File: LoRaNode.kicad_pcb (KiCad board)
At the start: 2 copper layers, 45 x 53 mm, 34 parts, among them J1 Conn_01x09, J2 Conn_01x03, J3 Conn_01x01, J4 ISP, J5 Conn_01x06, J6 Conn_01x01, J8 D2, J9 D3, SW1 SW_Push, U1 RFM95W-868S2, U4 ATMEGA328P-AU, Y1 8MHz HC5032/4

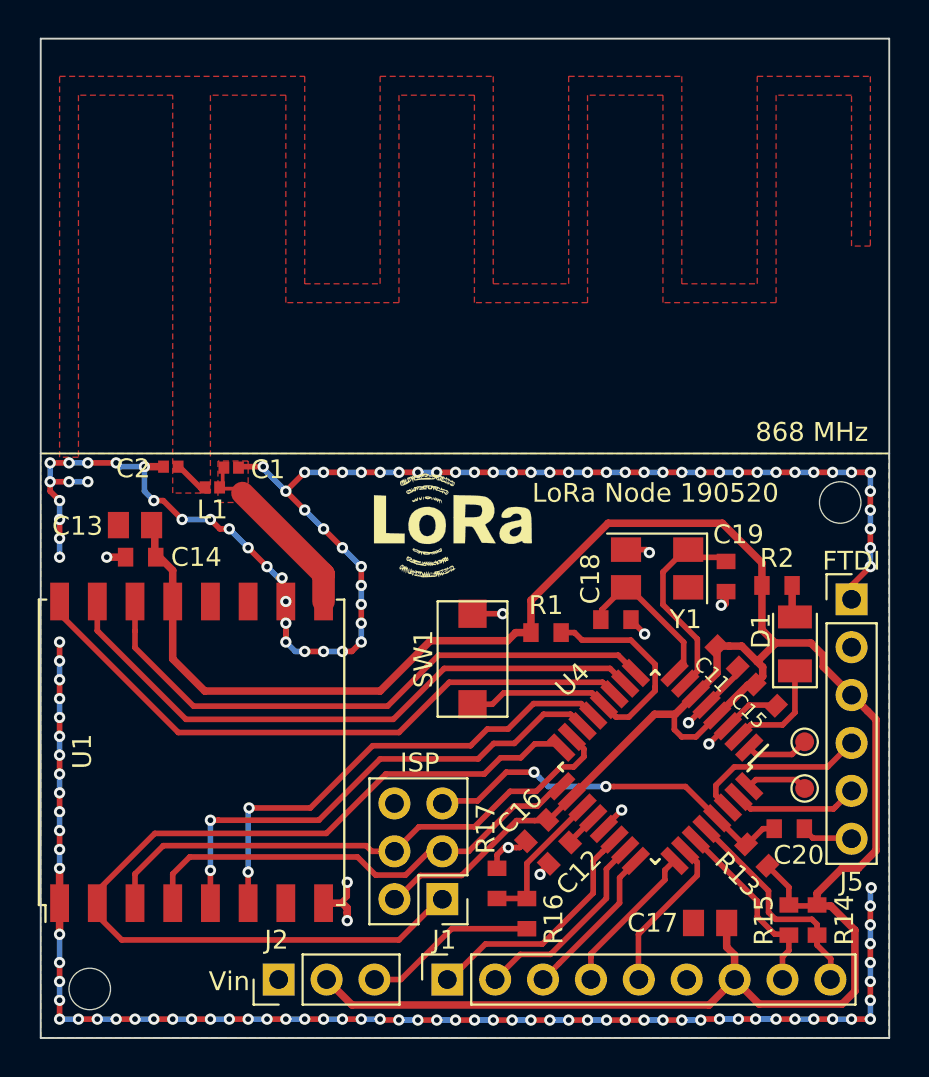
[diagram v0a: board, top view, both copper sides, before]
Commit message: Anotation reset, added BOM
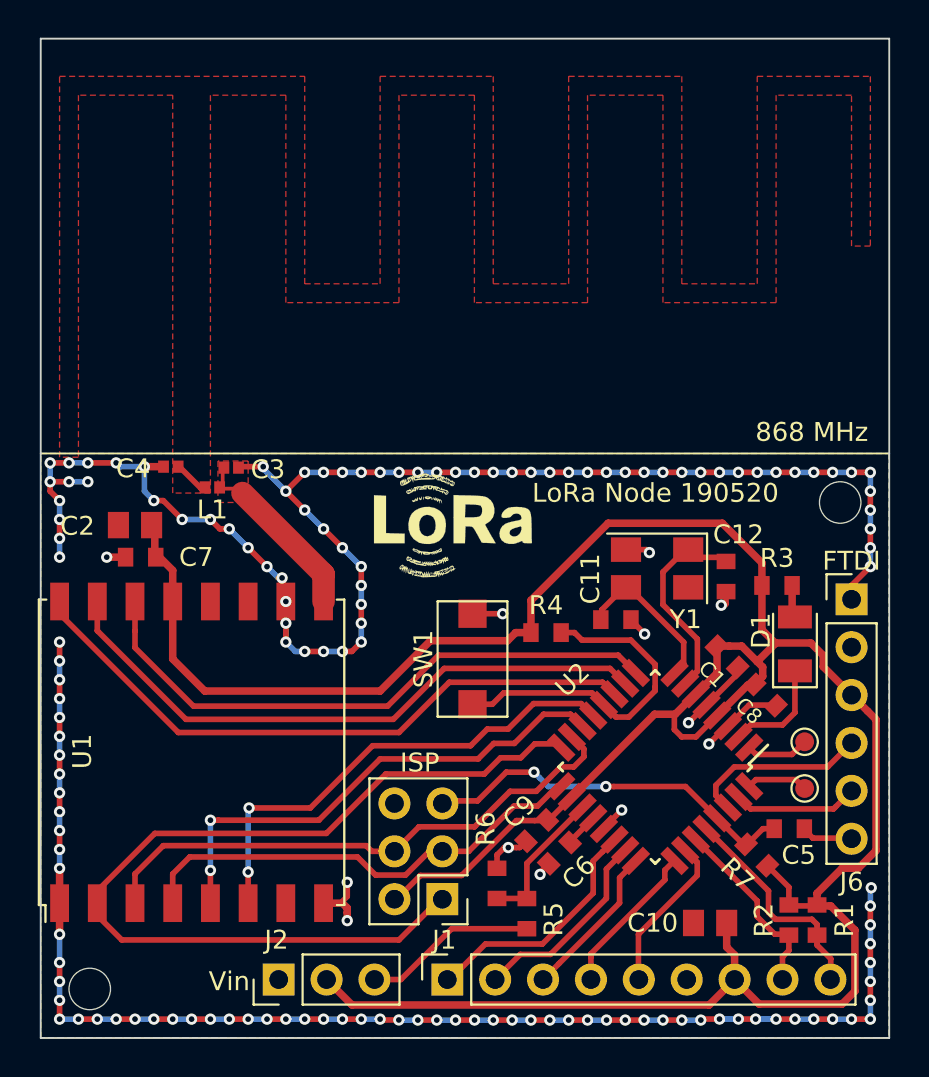
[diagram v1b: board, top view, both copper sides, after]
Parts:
- renumbered C11 to C1, C17 to C10, C18 to C11, C19 to C12, C13 to C2, C1 to C3, C2 to C4, C20 to C5, C12 to C6, C14 to C7, C15 to C8, C16 to C9, J4 to J3, J8 to J4, J9 to J5, J5 to J6, J3 to J7, J6 to J8, R14 to R1, R15 to R2, R2 to R3, R1 to R4, R16 to R5, R17 to R6, R13 to R7, U4 to U2

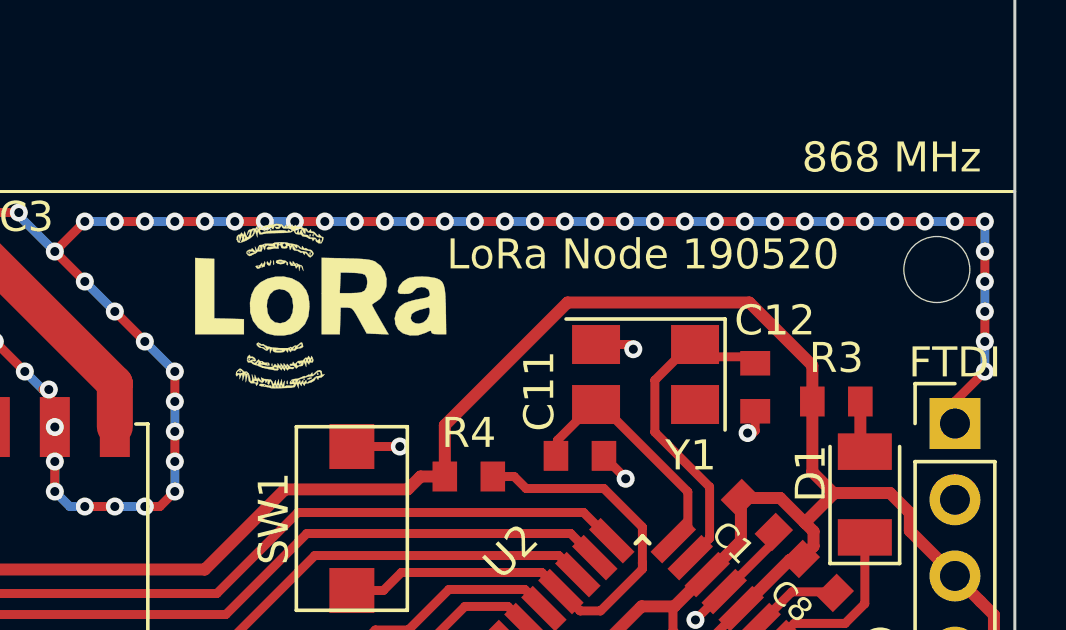
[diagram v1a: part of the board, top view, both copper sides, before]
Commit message: Corrected silk layer, removed old footprint files
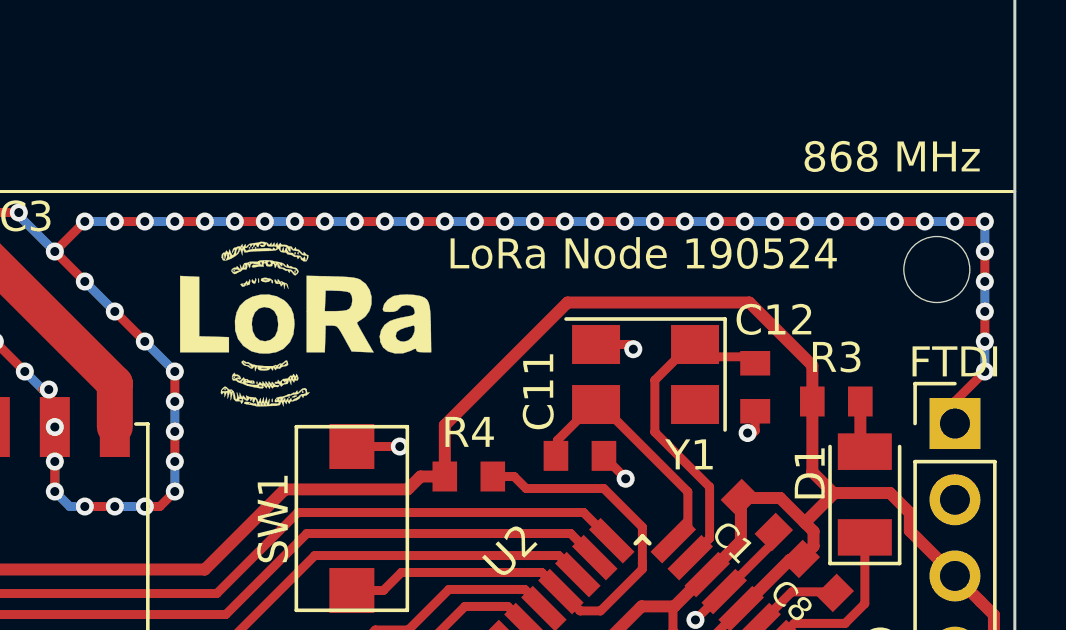
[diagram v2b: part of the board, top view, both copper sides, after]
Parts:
- added G***: RiskeLogo, kicad-footprints-master:RiskeLogo, B.Cu at (135.6, 94.6)
- moved G*** 0.78 mm to (148.8, 92.8)
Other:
- board text added: "LoRa Node 190524"
- board text removed: "LoRa Node 190520"
